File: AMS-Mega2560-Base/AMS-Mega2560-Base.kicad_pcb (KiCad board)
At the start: 4 copper layers, 168.7 x 106.7 mm, 191 parts, among them IC10 LM2597MX-ADJ_NOPB, IC11 LM2597M-3.3_NOPB, IC12 OPA2340PA, IC13 MAX764CPA+, IC14 LM2917N-8_NOPB, IC16 DS3231SN#, IC17 MAX232CPE+, IC19 MAX6326UR31+T, IC20 OPA4340UA, IC6 OPA4340UA, IC7 LTV-846S, IC9 LM2670SX-5.0_NOPB, J1 Conn_01x03, J2 Conn_01x03, J21 Screw_Terminal_01x03, J22 Conn_01x07, J23 Conn_01x02, J24 Conn_01x02, J3 Conn_01x08, J31 Conn_01x02, J4 Sense1, J5 Sense2, J6 AdafruitUltimateGPS, J7 Conn_02x03_Odd_Even, J8 Conn_01x03, K1 DIP05-1A72-12L, P1 Power, P10 CONN_01X01, P11 CONN_01X01, P12 CONN_01X01, P13 CONN_01X01, P2 Analog, P3 Analog, P4 Digital, P5 PWM, P6 PWM, P7 Communication, P8 CONN_01X01, P9 CONN_01X01, Q1 2N7000, Q10 IRF9Z34NPBF, Q11 2N7000, Q12 2N7000, Q13 IRF9Z34NPBF, Q14 IRF9Z34NPBF, Q15 2N7000, Q16 2N7000, Q17 IRF9Z34NPBF, Q18 IRF9Z34NPBF, Q19 2N7000, Q2 2N7000, Q20 IRF9Z34NPBF, Q21 IRF9Z34NPBF, Q22 IRF9610PBF-BE3, Q23 2N7000, Q24 BS250, Q25 2N7000, Q3 2N7000, Q4 2N7000, Q5 2N7000, Q6 IRF9Z34NPBF, Q7 2N7000, Q8 2N7000, Q9 IRF9Z34NPBF, T1 Conn_01x08, T2 Conn_01x08, T3 Conn_01x08, T4 Conn_01x08, T5 Conn_01x08, T6 Conn_01x08, U1 BK_HTC-15M, U2 TL431LP, U3 S8411-45R

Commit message: updated SD Card Detect resistor to be 47k vs 50k
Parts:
- R1: value 50K -> 47K
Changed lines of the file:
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@@
       (effects (font (size 1 1) (thickness 0.15)))
     )
-    (fp_text value "50K" (at 1.27 2.37 90) (layer "F.Fab")
+    (fp_text value "47K" (at 1.27 2.37 90) (layer "F.Fab")
       (effects (font (size 1 1) (thickness 0.15)))
     )

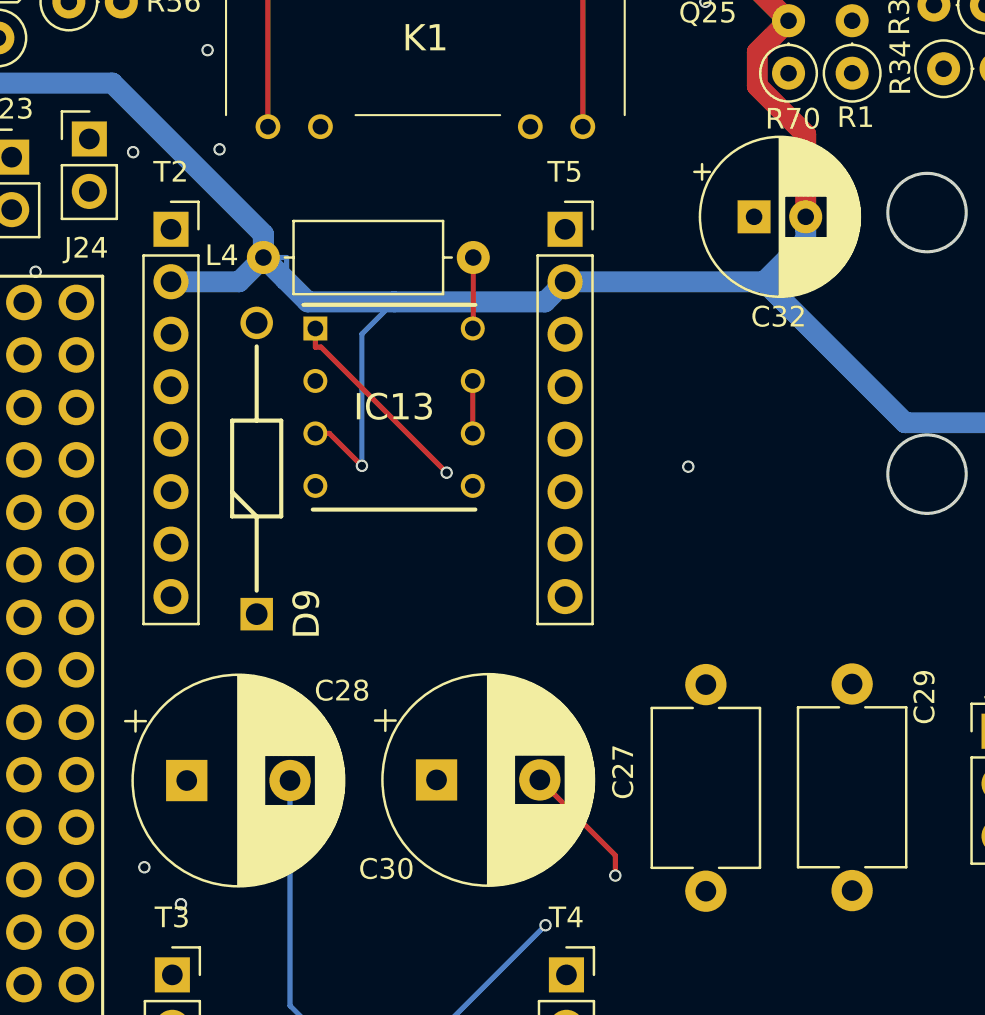
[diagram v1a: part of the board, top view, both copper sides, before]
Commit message: updating some values and footprints. needs to have the routing tweaked
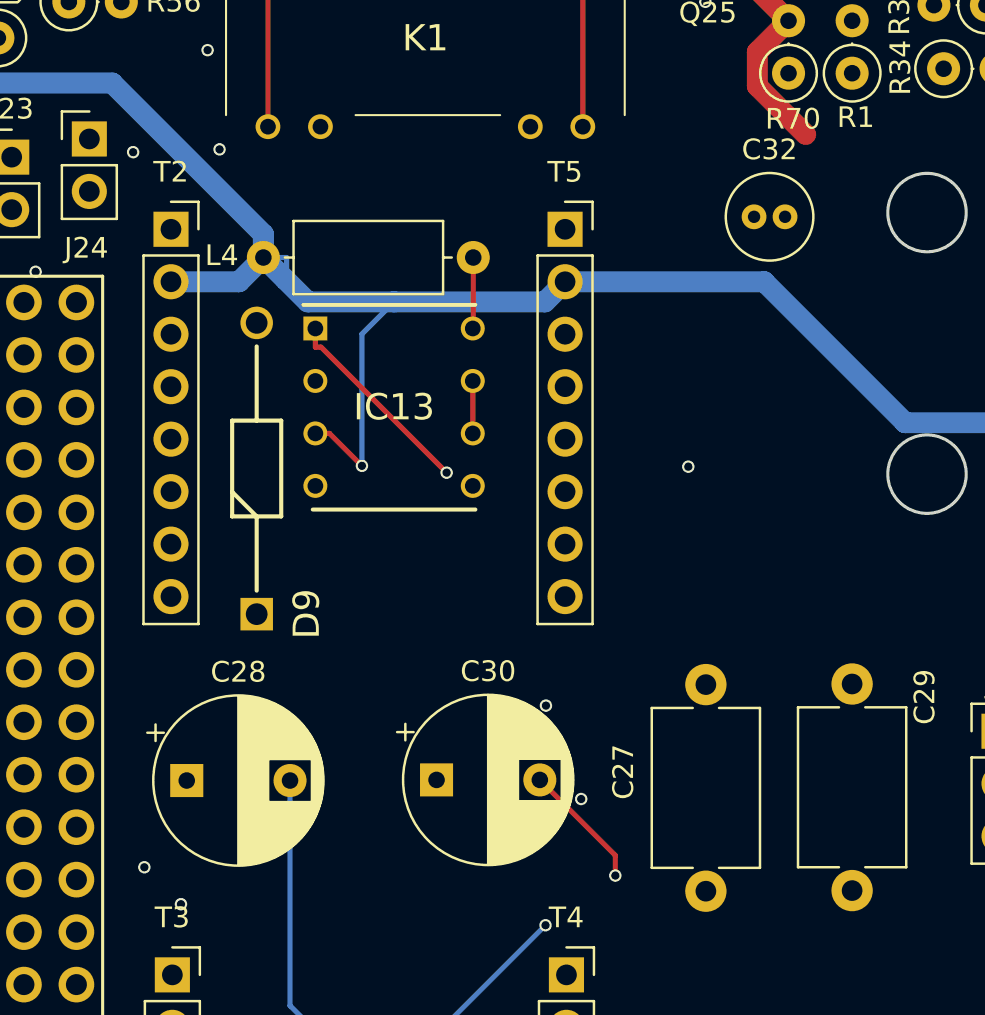
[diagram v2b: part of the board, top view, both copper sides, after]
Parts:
- C28, C30: footprint Capacitor_THT:CP_Radial_D10.0mm_P5.00mm -> Capacitor_THT:CP_Radial_D8.0mm_P5.00mm
- C32: footprint Capacitor_THT:CP_Radial_D7.5mm_P2.50mm -> Capacitor_THT:C_Radial_D4.0mm_H5.0mm_P1.50mm
- L4: value L -> 47uH
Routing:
- net GND: track 971.3 -> 960.8 mm
- net Net-(C32-Pad1): track 26.9 -> 21.3 mm

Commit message: still working on the fixes.
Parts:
- removed RV4: 500k, Potentiometer_THT:Potentiometer_Bourns_3296W_Vertical
- added R2: 100K, Resistor_THT:R_Axial_DIN0207_L6.3mm_D2.5mm_P2.54mm_Vertical, F.Cu at (113.9, 33.1)
- added R20: 100K, Resistor_THT:R_Axial_DIN0207_L6.3mm_D2.5mm_P2.54mm_Vertical, F.Cu at (113.9, 29.0)
- added R3: 100K, Resistor_THT:R_Axial_DIN0207_L6.3mm_D2.5mm_P2.54mm_Vertical, F.Cu at (120.1, 29.0)
- added R36: 100K, Resistor_THT:R_Axial_DIN0207_L6.3mm_D2.5mm_P2.54mm_Vertical, F.Cu at (132.9, 33.7)
- added R4: 100K, Resistor_THT:R_Axial_DIN0207_L6.3mm_D2.5mm_P2.54mm_Vertical, F.Cu at (120.1, 33.1)
- added R60: 100K, Resistor_THT:R_Axial_DIN0207_L6.3mm_D2.5mm_P2.54mm_Vertical, F.Cu at (139.0, 29.0)
- added R71: 100K, Resistor_THT:R_Axial_DIN0207_L6.3mm_D2.5mm_P2.54mm_Vertical, F.Cu at (139.1, 33.8)
- added R72: 100K, Resistor_THT:R_Axial_DIN0207_L6.3mm_D2.5mm_P2.54mm_Vertical, F.Cu at (132.9, 29.0)
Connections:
- net ComRX renamed Com1RX
- net ComTX renamed Com1TX
- IC17 pad 10: unconnected-(IC17-Pad10) -> Com2TX
- IC17 pad 7: unconnected-(IC17-Pad7) -> /Sheet6152913C/RSCOM2TX
- IC17 pad 8: unconnected-(IC17-Pad8) -> /Sheet6152913C/RSCOM2RX
- IC17 pad 9: unconnected-(IC17-Pad9) -> Com2RX
- IC20 pad 12: /BufferedADC/ADCIN4 -> Sense1-3
- P4 pad 30: unconnected-(P4-Pad30) -> SWSCLK
- P4 pad 32: unconnected-(P4-Pad32) -> SWMISO
- P4 pad 34: unconnected-(P4-Pad34) -> SWMOSI
- P7 pad 1: GPSTX -> GPSRX
- P7 pad 2: GPSRX -> GPSTX
- P7 pad 5: unconnected-(P7-Pad5) -> Com2TX
- P7 pad 6: unconnected-(P7-Pad6) -> Com2RX
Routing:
- net GND: track 960.8 -> 233.4 mm, vias 28 -> 0
- net +5V: track 534.0 -> 19.6 mm, vias 3 -> 0
- net +10V: track 208.0 -> 0.00 mm
- net +3.3VP: track 217.4 -> 24.5 mm, vias 2 -> 0
- net RTDSCLK: track 171.3 -> 0.00 mm, vias 1 -> 0
- net RTDMISO: track 167.8 -> 0.00 mm
- net RTDMOSI: track 165.6 -> 0.00 mm, vias 1 -> 0
- net Net-(J31-Pad1): track 158.0 -> 0.00 mm, vias 1 -> 0
- net Sense2-10: track 144.7 -> 0.00 mm, vias 1 -> 0
- net Sense1-3: track 143.9 -> 0.00 mm, vias 2 -> 0
- net SCL: track 142.2 -> 0.00 mm, vias 1 -> 0
- net SDA: track 133.3 -> 0.00 mm, vias 2 -> 0
- net Sense2-1: track 129.2 -> 0.00 mm, vias 4 -> 0
- net Sense2-4: track 122.1 -> 0.00 mm, vias 3 -> 0
- net Logging: track 120.6 -> 0.00 mm, vias 3 -> 0
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- removed copper zone on B.Cu, net GND

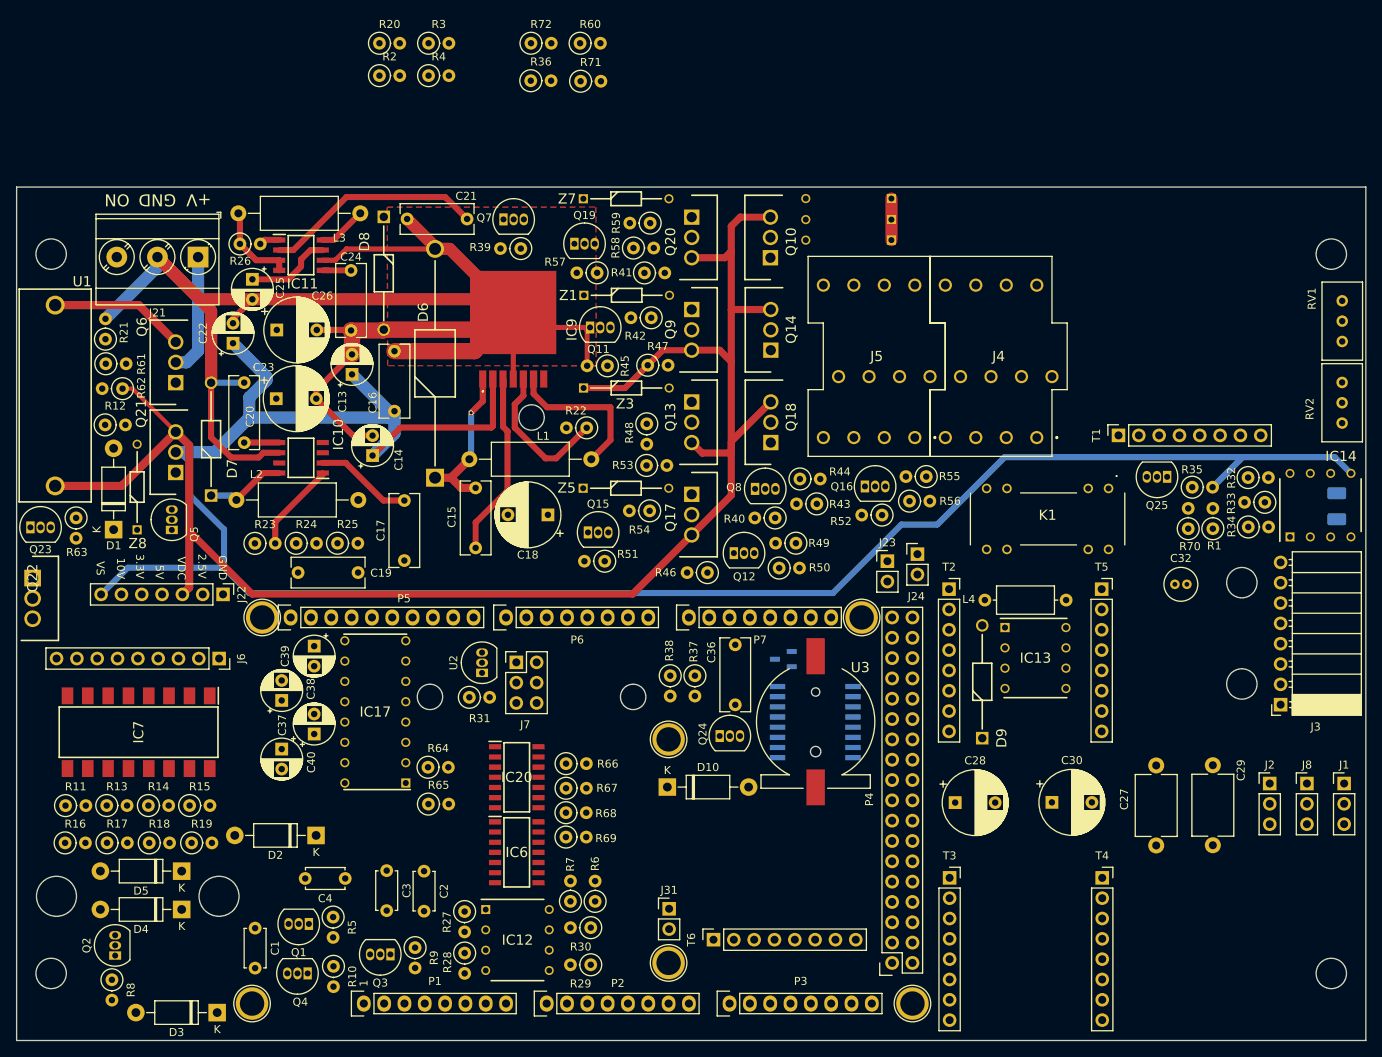
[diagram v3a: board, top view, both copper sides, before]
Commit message: just need to route the 5V power around the board before i figure out what to do with the other serial port
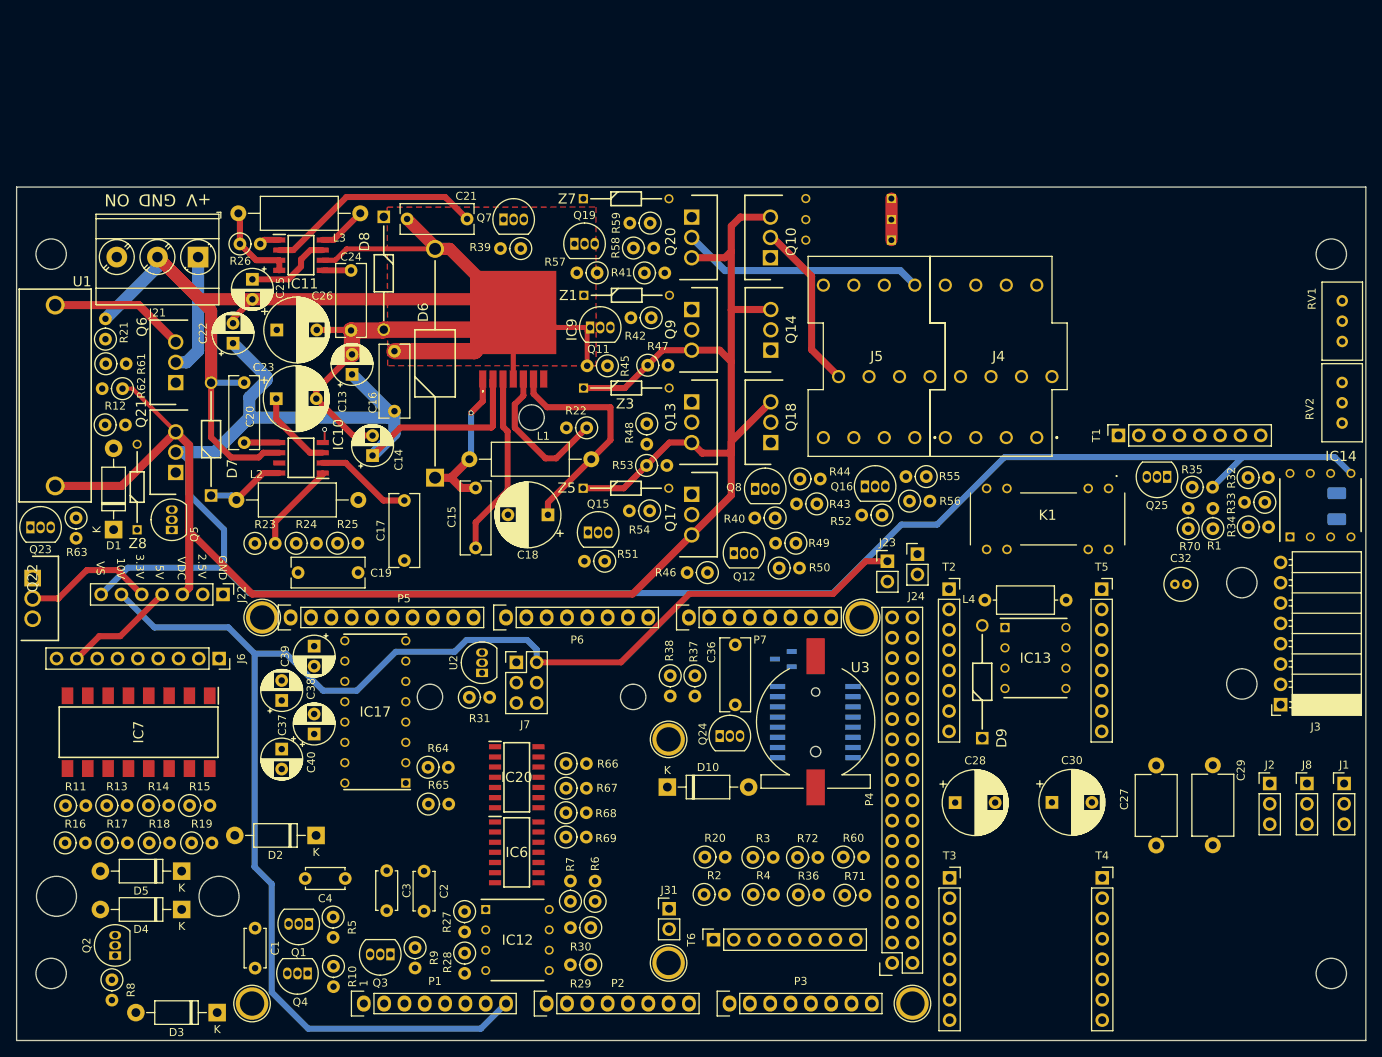
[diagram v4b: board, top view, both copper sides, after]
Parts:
- moved R2 110.1 mm to (154.5, 135.4)
- moved R4 110.1 mm to (160.7, 135.4)
- moved R20 109.6 mm to (154.6, 130.7)
- moved R3 109.5 mm to (160.6, 130.8)
- moved R36 107.1 mm to (166.3, 135.5)
- moved R72 107.1 mm to (166.2, 130.8)
- moved R71 107.0 mm to (172.1, 135.5)
- moved R60 106.9 mm to (171.9, 130.7)
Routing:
- net GND: track 233.4 -> 652.2 mm
- net +10V: track 0.00 -> 258.5 mm
- net Sense2-12: track 0.00 -> 41.1 mm
- net Sense2-3: track 0.00 -> 30.4 mm
- net Sense2-9: track 0.00 -> 29.2 mm
- net Sense2-6: track 0.00 -> 28.5 mm
- net Net-(C19-Pad1): track 0.00 -> 23.6 mm, vias 0 -> 1
- net +5V: track 19.6 -> 42.8 mm
- net Sense2-5: track 0.00 -> 21.1 mm
- net Sense2-11: track 0.00 -> 21.1 mm
- net +3.3VA: track 0.00 -> 16.4 mm
- net +VDC: track 247.2 -> 263.1 mm
- net Sense2-8: track 0.00 -> 14.7 mm

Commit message: wip while i get set to autoroute
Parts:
- added J9: Conn_01x03, Connector_PinHeader_2.54mm:PinHeader_1x03_P2.54mm_Vertical, F.Cu at (110.8, 129.3)
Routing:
- net GND: track 652.2 -> 1210.5 mm
- net +5V: track 42.8 -> 507.9 mm
- net +VDC: track 263.1 -> 308.2 mm
- net Net-(Q13-Pad1): track 0.00 -> 12.1 mm
- net Net-(Q20-Pad1): track 0.00 -> 11.1 mm
- net Net-(Q9-Pad1): track 0.00 -> 10.3 mm
- net Net-(C31-Pad1): track 0.00 -> 4.22 mm
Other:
- board text added: "AFR1"
- board text added: "AFR2"
- board text added: "ALT"
- board text added: "Alarm"
- board text added: "FP1"
- board text added: "FP2"
- board text added: "IN1"
- board text added: "In2"
- board text added: "In3"
- board text added: "LED1"
- board text added: "LED2"
- board text added: "Log"
- board text added: "OP"
- board text added: "OUT1"
- board text added: "OUT2"
- board text added: "OUT3"
- board text added: "OUT4"
- board text added: "RX"
- board text added: "SADC"
- board text added: "SCL"
- board text added: "SDA"
- board text added: "TP"
- board text added: "TX"
- board text added: "Tach"

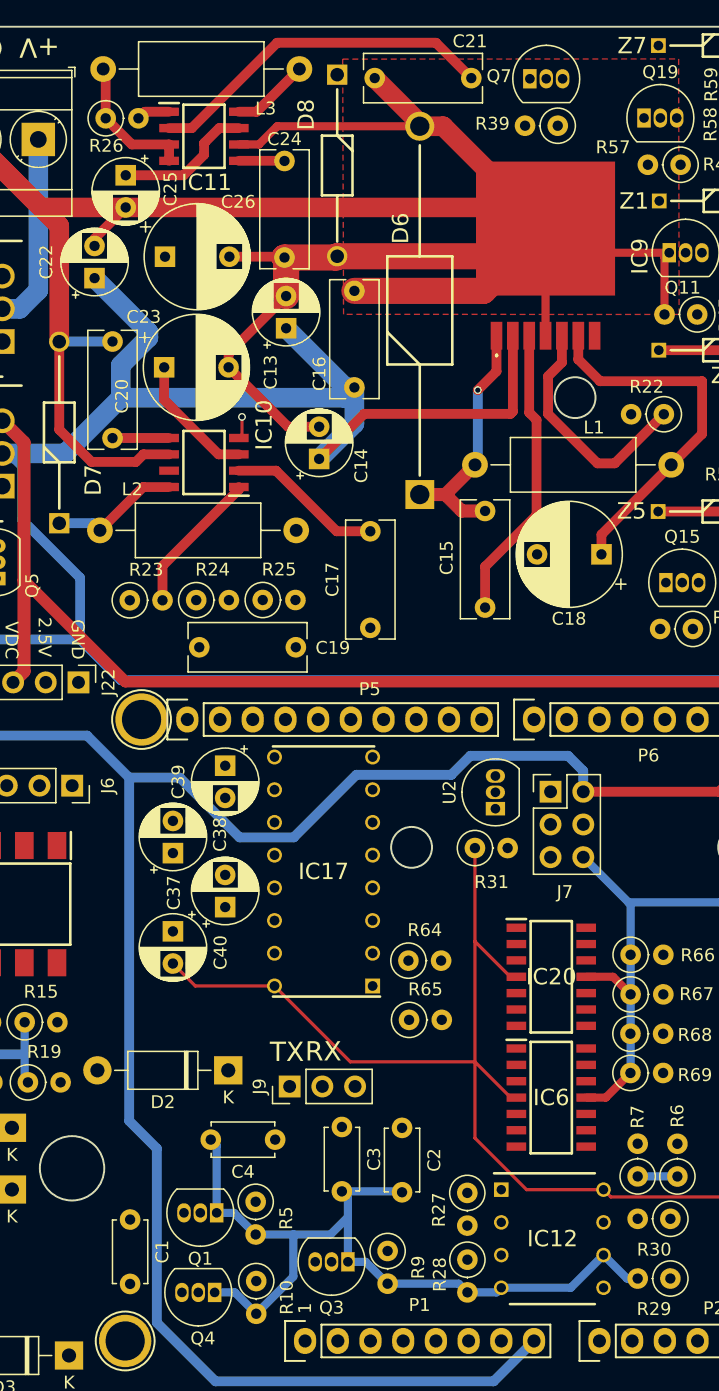
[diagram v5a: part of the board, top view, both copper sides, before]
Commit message: fixed 2.5v source. added gnd fill area to keep the noise down.
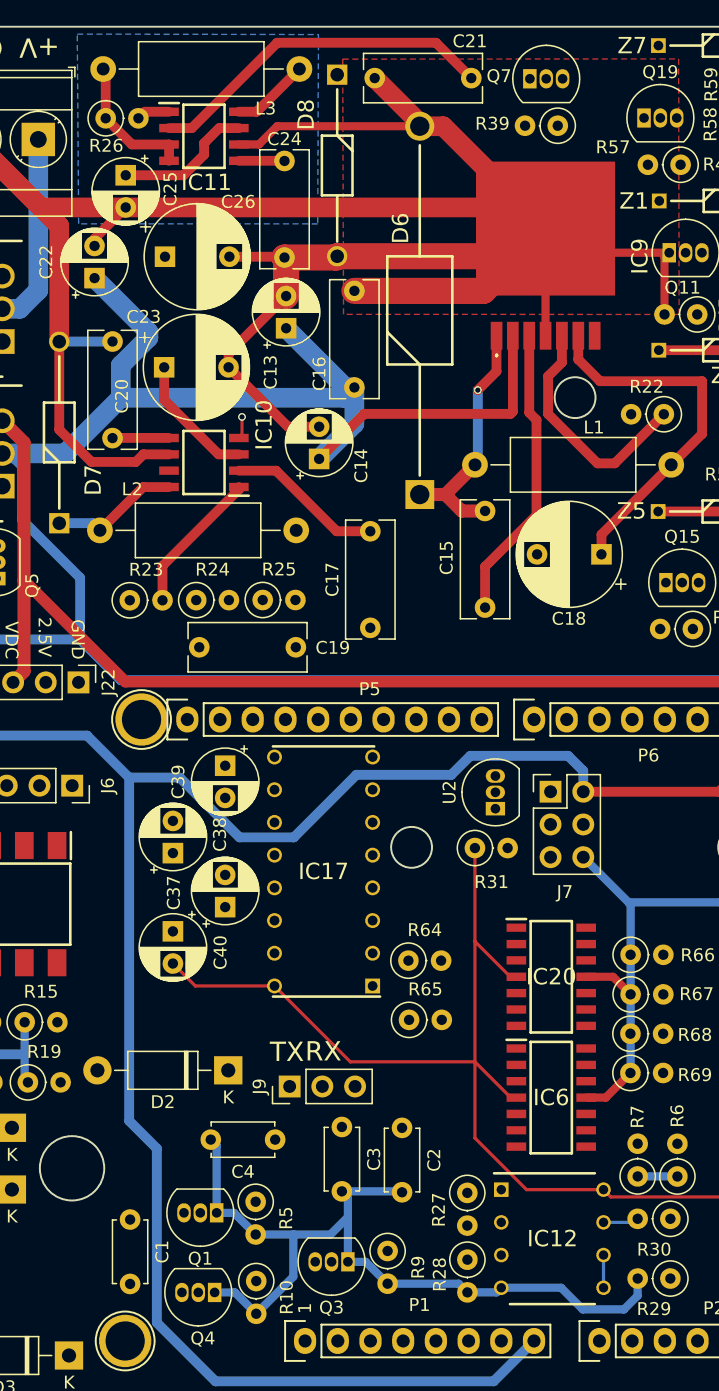
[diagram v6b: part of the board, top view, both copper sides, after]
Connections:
- IC12 pad 6: GND -> Net-(IC12-Pad5)
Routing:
- net +2V5: track 0.00 -> 2.77 mm
- net Net-(IC12-Pad5): track 0.00 -> 2.54 mm
- net GND: track 1210.5 -> 1211.2 mm
- added copper zone on B.Cu, net GND

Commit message: ready to autoroute
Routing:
- net Net-(Q18-Pad1): track 0.00 -> 49.5 mm
- net Net-(Q14-Pad1): track 0.00 -> 44.2 mm
- net GND: track 1211.2 -> 1200.2 mm
- net Net-(Q10-Pad1): track 0.00 -> 9.23 mm

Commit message: autorouted needs to be DRC'ed and fix whatever the autorouter did horribly
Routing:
- net RTDMISO: track 0.00 -> 183.0 mm
- net +3.3VP: track 24.5 -> 200.1 mm
- net Sense2-10: track 0.00 -> 172.6 mm, vias 0 -> 2
- net RTDMOSI: track 0.00 -> 172.0 mm, vias 0 -> 1
- net RTDSCLK: track 0.00 -> 171.6 mm, vias 0 -> 2
- net SDA: track 0.00 -> 142.5 mm, vias 0 -> 2
- net Sense1-3: track 0.00 -> 136.7 mm, vias 0 -> 1
- net SCL: track 0.00 -> 134.4 mm, vias 0 -> 1
- net Sense1-12: track 0.00 -> 133.5 mm, vias 0 -> 4
- net Sense1-9: track 0.00 -> 131.5 mm, vias 0 -> 2
- net Sense2-4: track 0.00 -> 130.9 mm, vias 0 -> 2
- net Sense1-6: track 0.00 -> 129.8 mm, vias 0 -> 3
- net GND: track 1200.2 -> 1328.0 mm, vias 0 -> 10
- net Net-(J31-Pad1): track 0.00 -> 121.9 mm, vias 0 -> 1
- net Sense1-1: track 0.00 -> 121.2 mm, vias 0 -> 2
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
